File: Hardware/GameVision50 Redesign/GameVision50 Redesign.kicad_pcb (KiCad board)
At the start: 2 copper layers, 54.9 x 59.9 mm, 2 parts

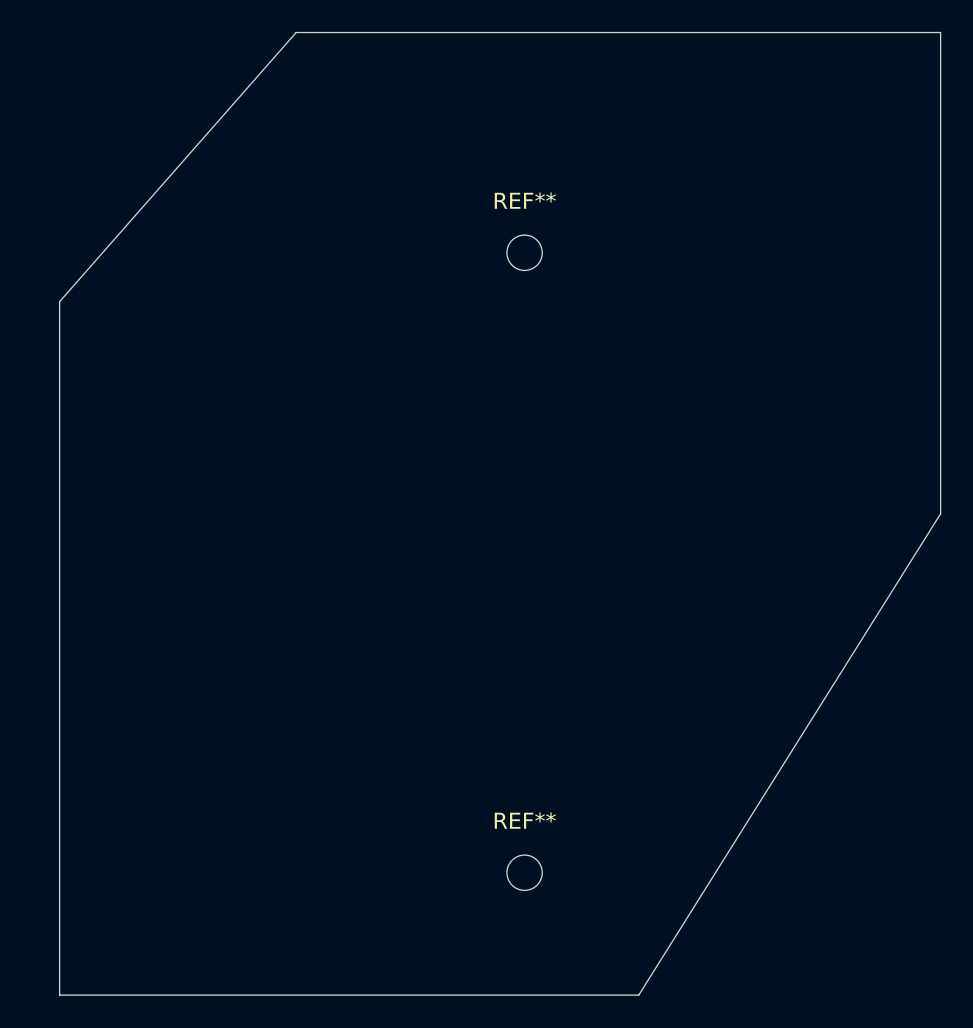
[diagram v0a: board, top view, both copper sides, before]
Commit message: better footprint layout and 3d model of oscillator
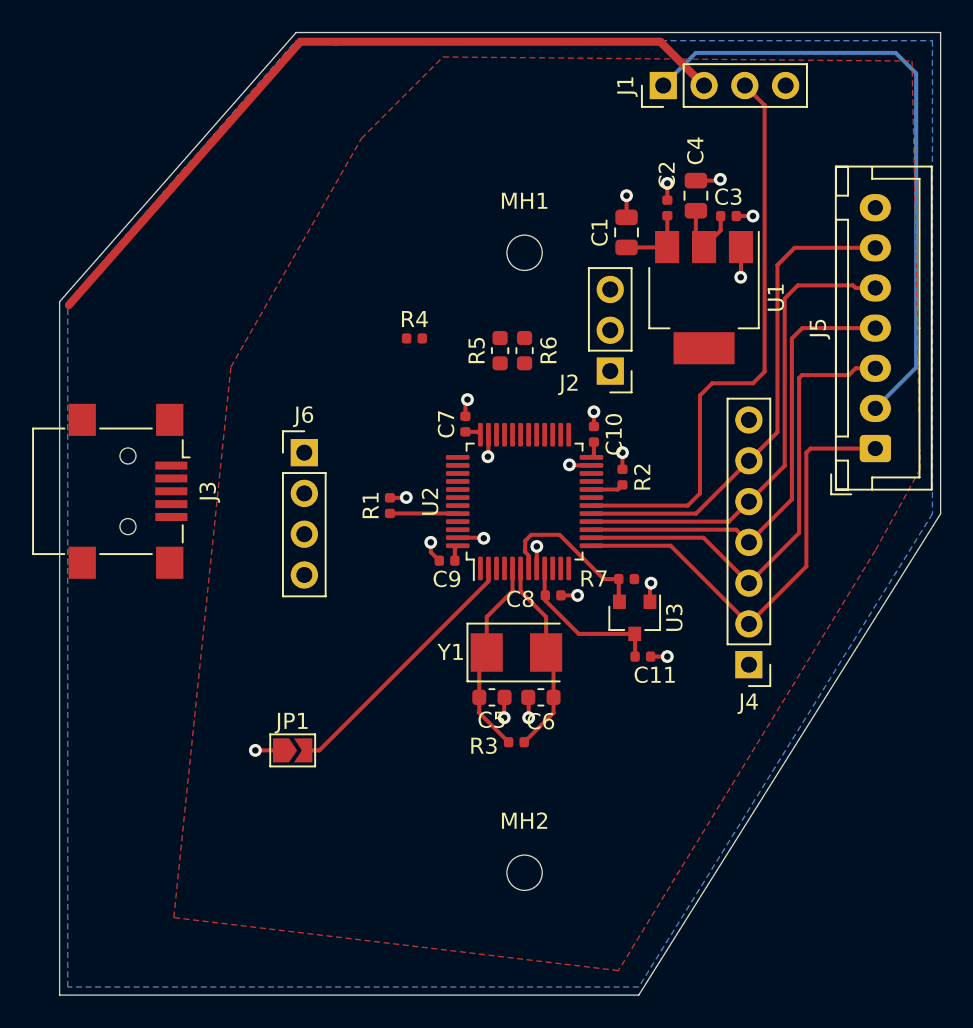
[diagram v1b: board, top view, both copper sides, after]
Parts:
- added C1: 10μF, Capacitor_SMD:C_0805_2012Metric, F.Cu at (136.9, 63.2)
- added C10: 100nF, Capacitor_SMD:C_0402_1005Metric, F.Cu at (134.9, 75.8)
- added C11: 100nF, Capacitor_SMD:C_0402_1005Metric, F.Cu at (137.9, 89.7)
- added C2: 100nF, Capacitor_SMD:C_0402_1005Metric, F.Cu at (139.4, 61.7)
- added C3: 100nF, Capacitor_SMD:C_0402_1005Metric, F.Cu at (143.3, 62.2)
- added C4: 10μF, Capacitor_SMD:C_0805_2012Metric, F.Cu at (141.2, 61.0)
- added C5: 20pF, Capacitor_SMD:C_0603_1608Metric, F.Cu at (128.5, 92.2)
- added C6: 20pF, Capacitor_SMD:C_0603_1608Metric, F.Cu at (131.6, 92.2)
- added C7: 100nF, Capacitor_SMD:C_0402_1005Metric, F.Cu at (126.9, 75.2)
- added C8: 100nF, Capacitor_SMD:C_0402_1005Metric, F.Cu at (132.3, 85.9)
- added C9: 100nF, Capacitor_SMD:C_0402_1005Metric, F.Cu at (125.7, 83.7)
- added J1: Reset/Power, Connector_PinHeader_2.54mm:PinHeader_1x04_P2.54mm_Vertical, F.Cu at (139.2, 54.1)
- added J2: Potentiometer, Connector_PinHeader_2.54mm:PinHeader_1x03_P2.54mm_Vertical, F.Cu at (135.9, 71.9)
- added J3: USB_B_Mini, Connector_USB:USB_Mini-B_Lumberg_2486_01_Horizontal, F.Cu at (105.9, 79.4)
- added J4: Test Points, Connector_PinHeader_2.54mm:PinHeader_1x07_P2.54mm_Vertical, F.Cu at (144.5, 90.2)
- added J5: Controller, Connector_JST:JST_XH_B7B-XH-A_1x07_P2.50mm_Vertical, F.Cu at (152.4, 76.7)
- added J6: STLink, Connector_PinHeader_2.54mm:PinHeader_1x04_P2.54mm_Vertical, F.Cu at (116.8, 77.0)
- added JP1: Control Mode, Jumper:SolderJumper-2_P1.3mm_Open_TrianglePad1.0x1.5mm, F.Cu at (116.1, 95.5)
- added R1: 100KΩ, Resistor_SMD:R_0402_1005Metric, F.Cu at (122.2, 80.3)
- added R2: 100KΩ, Resistor_SMD:R_0402_1005Metric, F.Cu at (136.7, 78.5)
- added R3: 1M, Resistor_SMD:R_0402_1005Metric, F.Cu at (130.0, 95.0)
- added R4: 1.5KΩ, Resistor_SMD:R_0402_1005Metric, F.Cu at (123.7, 69.8)
- added R5: 20Ω, Resistor_SMD:R_0603_1608Metric, F.Cu at (129.0, 70.6)
- added R6: 20Ω, Resistor_SMD:R_0603_1608Metric, F.Cu at (130.6, 70.6)
- added R7: 4.7KΩ, Resistor_SMD:R_0402_1005Metric, F.Cu at (136.9, 84.8)
- added U1: AMS1117-3.3, Package_TO_SOT_SMD:SOT-223-3_TabPin2, F.Cu at (141.7, 67.3)
- added U2: STM32F103C8Tx, Package_QFP:LQFP-48_7x7mm_P0.5mm, F.Cu at (130.6, 80.0)
- added U3: APX803S-29SA-7, Package_TO_SOT_SMD:SOT-23, F.Cu at (137.4, 87.2)
- added Y1: 8MHz, Crystal:Crystal_SMD_5032-2Pin_5.0x3.2mm, F.Cu at (130.0, 89.4)
- renumbered REF** to MH1, REF** to MH2
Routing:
- net /POWER: track 0.00 -> 48.1 mm
- net +5V: track 0.00 -> 43.5 mm
- net /RESET: track 0.00 -> 36.1 mm
- net /SCK2: track 0.00 -> 30.6 mm
- net /SCK1: track 0.00 -> 30.1 mm
- net /P2D0: track 0.00 -> 29.9 mm
- net /P1D0: track 0.00 -> 29.4 mm
- net /OUT0: track 0.00 -> 28.4 mm
- net GND: track 0.00 -> 25.5 mm, vias 0 -> 20
- net +3V3: track 0.00 -> 17.7 mm
- net /MODE: track 0.00 -> 16.6 mm
- net Net-(C5-Pad2): track 0.00 -> 12.4 mm
- net Net-(C6-Pad2): track 0.00 -> 12.4 mm
- net Net-(R7-Pad2): track 0.00 -> 10.4 mm
- net /BOOT0: track 0.00 -> 4.22 mm
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- added copper zone on F.Cu, net +3V3
- added copper zone on B.Cu, net GND
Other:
- net class Power added: clearance 0.3, trace_width 0.5, via_dia 0.8, via_drill 0.4
- board text added: "VDDA analog"

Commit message: exported version 1 of PCB to manufacture
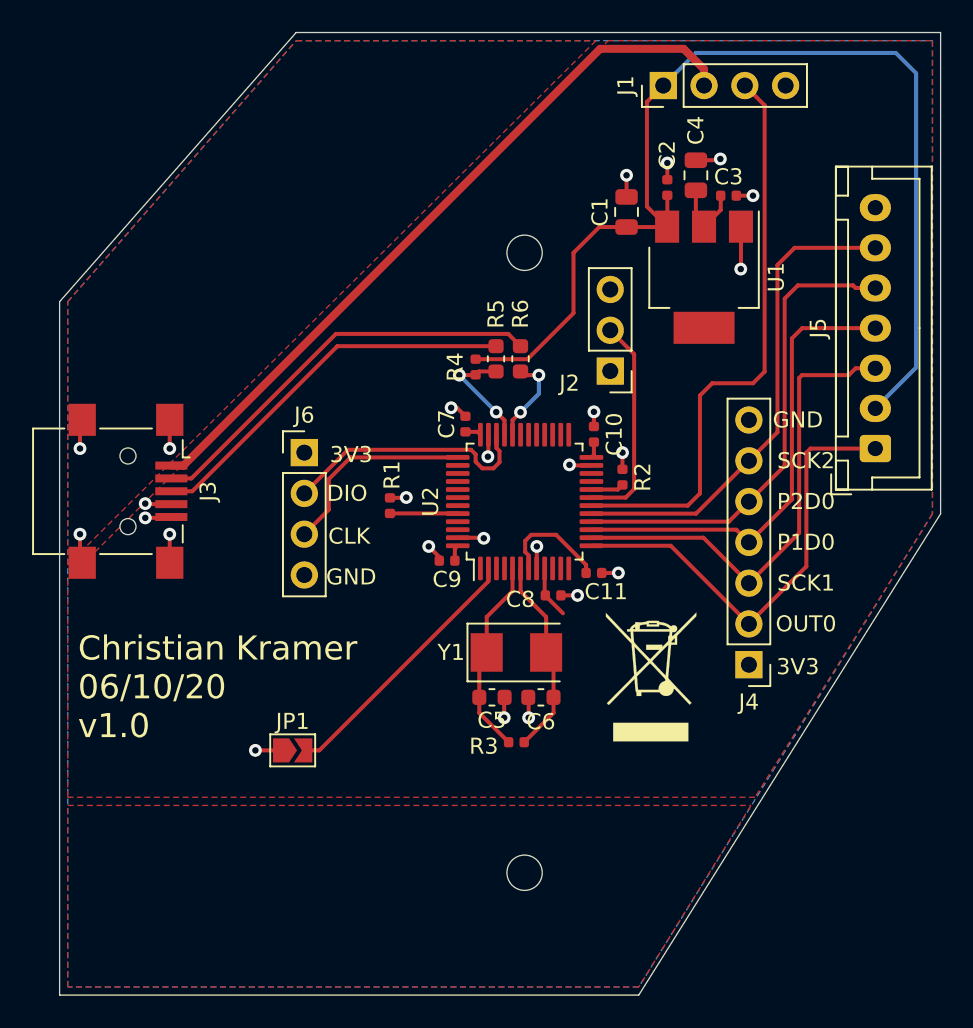
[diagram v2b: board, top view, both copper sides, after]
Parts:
- removed MH1, MH2: MountingHole_2.2mm_M2, MountingHole:MountingHole_2.2mm_M2
- removed R7: 4.7KΩ, Resistor_SMD:R_0402_1005Metric
- removed U3: APX803S-29SA-7, Package_TO_SOT_SMD:SOT-23
- added G***: LOGO, KiCad Footprints:Signature, F.Cu at (114.9, 104.9)
- added G***: LOGO, KiCad Footprints:GameVision Logo, F.Cu at (113.7, 62.4)
- added REF**: WEEE-Logo_5.6x8mm_SilkScreen, Symbol:WEEE-Logo_5.6x8mm_SilkScreen, F.Cu at (138.4, 90.9)
- added REF**: MountingHole_2.2mm_M2, MountingHole:MountingHole_2.2mm_M2, F.Cu at (130.6, 64.5)
- added REF**: MountingHole_2.2mm_M2, MountingHole:MountingHole_2.2mm_M2, F.Cu at (130.6, 103.1)
- moved C11 6.03 mm to (134.9, 84.5)
- moved R4 4.20 mm to (127.5, 71.6), turned to 270 degrees
- moved C1 1.27 mm to (136.9, 62.0)
- moved C2 1.27 mm to (139.4, 60.5)
- moved C4 1.27 mm to (141.2, 59.7)
- moved C3 1.27 mm to (143.3, 61.0)
- moved U1 1.27 mm to (141.7, 66.0)
- moved R5 0.57 mm to (128.8, 71.1)
- moved R6 0.57 mm to (130.3, 71.1)
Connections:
- C11 pad 2: +3V3 -> Net-(C11-Pad2)
- U2 pad 7: Net-(R7-Pad2) -> Net-(C11-Pad2)
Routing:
- net Net-(J3-Pad2): track 0.00 -> 25.8 mm
- net +5V: track 43.5 -> 68.2 mm
- net Net-(J3-Pad3): track 0.00 -> 24.0 mm
- net /SWDIO: track 0.00 -> 16.0 mm
- net Net-(J2-Pad2): track 0.00 -> 13.4 mm
- net /SWDCLK: track 0.00 -> 12.6 mm
- net Net-(R7-Pad2): track 10.4 -> 0.00 mm
- net GND: track 25.5 -> 34.5 mm, vias 20 -> 25
- net /USB_DP: track 0.00 -> 7.82 mm, vias 0 -> 2
- net +3V3: track 17.7 -> 10.4 mm
- net Net-(C11-Pad2): track 0.00 -> 7.07 mm
- net /USB_DM: track 0.00 -> 5.63 mm, vias 0 -> 2
- net /POWER: track 48.1 -> 45.5 mm
- added copper zone on F.Cu, net (none)
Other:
- board text added: "3V3"
- board text added: "Additional Info"
- board text added: "CLK"
- board text added: "Christian Kramer 06/10/20 v1.0"
- board text added: "DIO"
- board text added: "GND"
- board text added: "Info"
- board text added: "OUT0"
- board text added: "P1D0"
- board text added: "P2D0"
- board text added: "SCK1"
- board text added: "SCK2"
- board text added: "Signature"
